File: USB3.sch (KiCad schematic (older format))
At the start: 45 parts

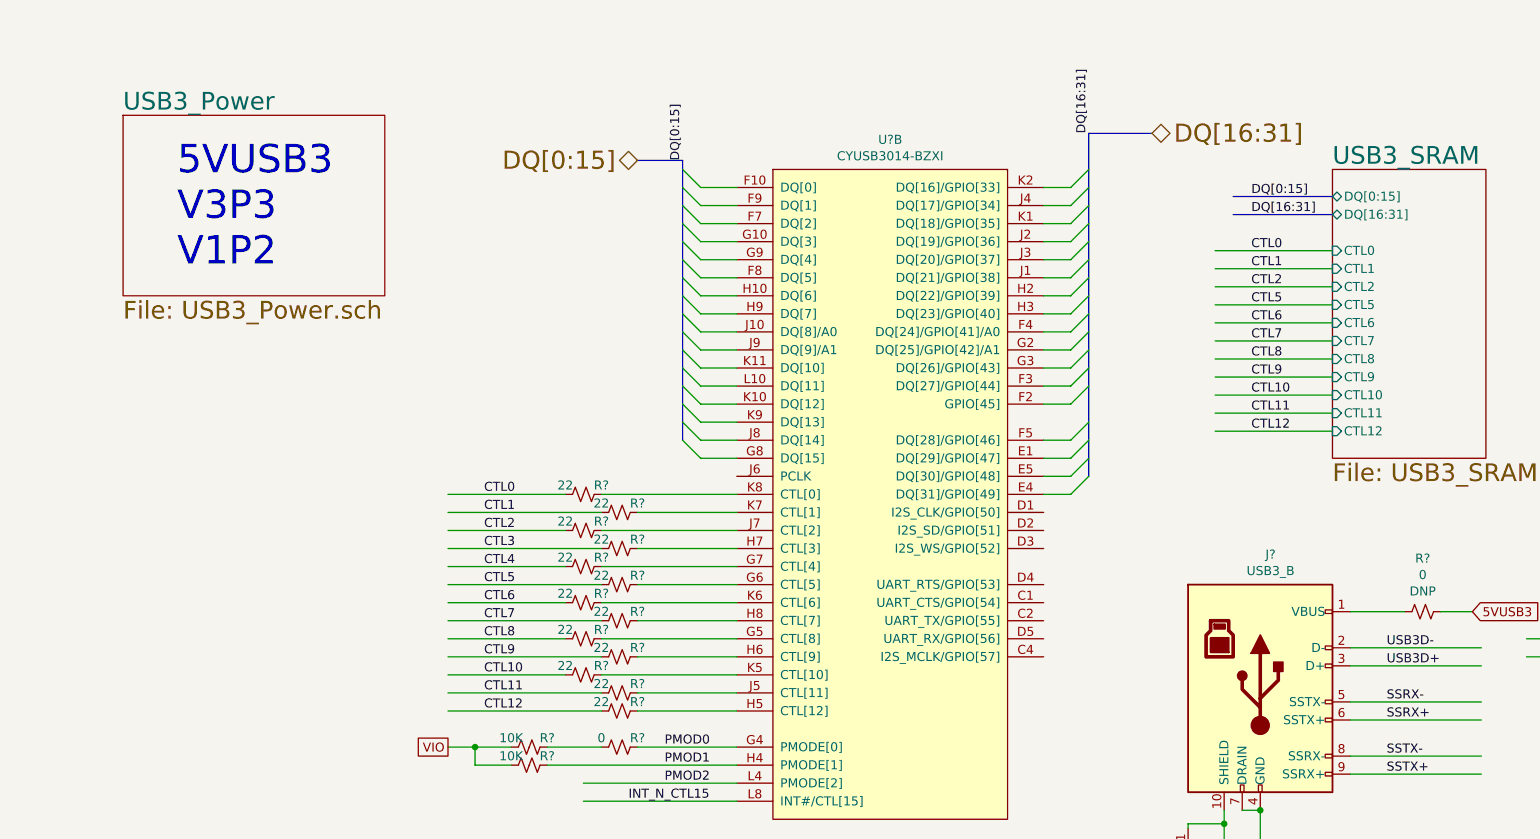
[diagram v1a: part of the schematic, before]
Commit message: Rearranged the top sheet blocks modified hir. pins in few blocks
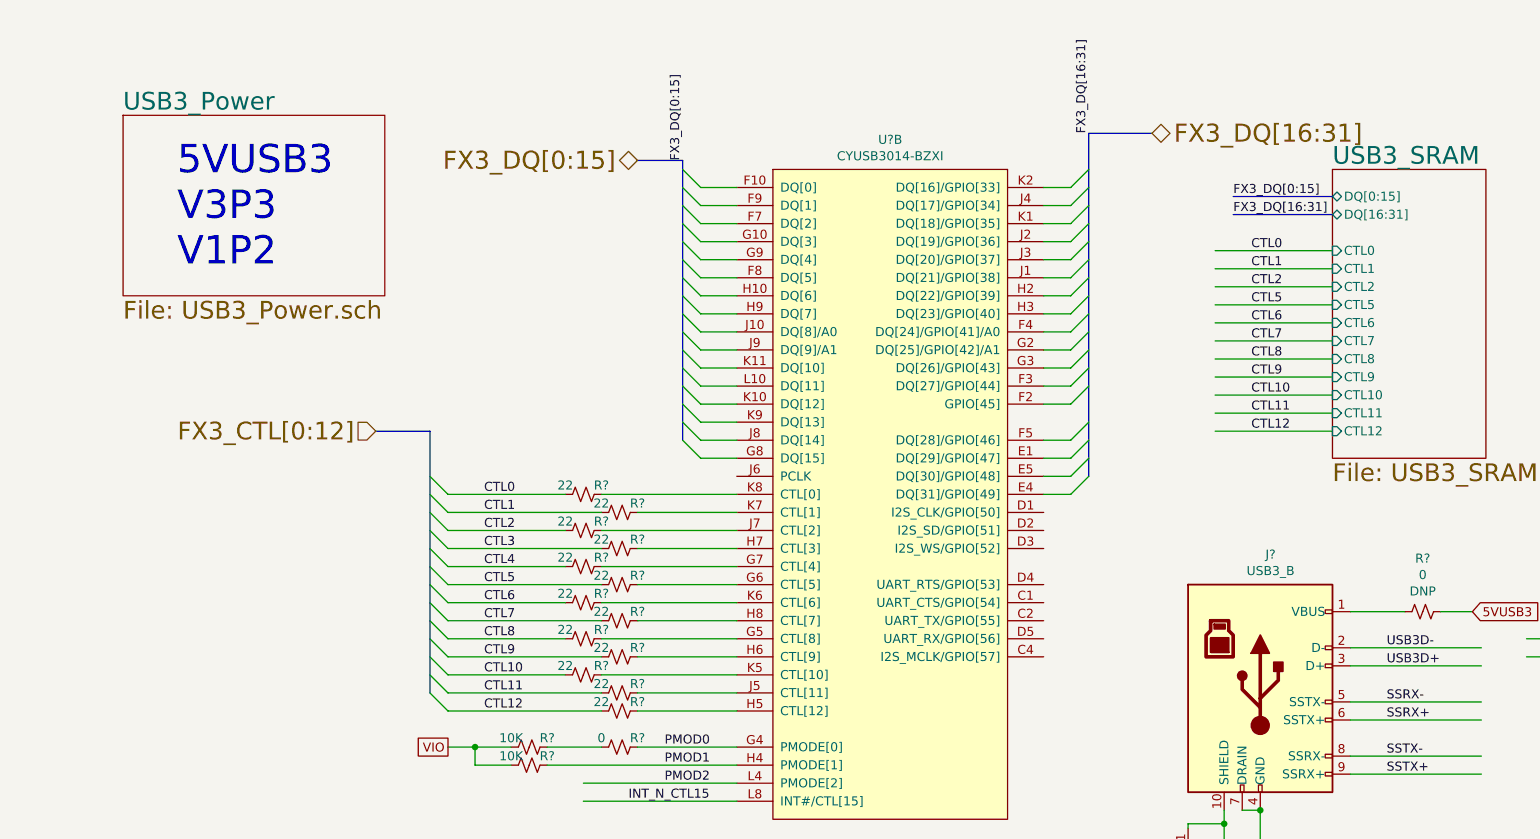
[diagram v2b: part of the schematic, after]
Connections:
- net labels added: FX3_CTL[0:12], FX3_DQ[0:15], FX3_DQ[16:31]
- net labels removed: DQ[0:15], DQ[16:31]
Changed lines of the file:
@@
 $Descr A4 11693 8268
 encoding utf-8
-Sheet 15 22
+Sheet 13 22
 Title "CGMPCX1006"
 Date "2021-02-03"
@@
 	6100 1050 6450 1050
 Text HLabel 6450 1050 2    100  BiDi ~ 0
-DQ[16:31]
+FX3_DQ[16:31]
 $Comp
 L GM_Memory_EEPROM:M24M02-DRMN6TP IC?
@@
 Text Notes 1050 1800 0    157  ~ 0
 5VUSB3\nV3P3\nV1P2
-Text Label 6100 1050 1    50   ~ 0
-DQ[16:31]
-Text Label 3850 1200 1    50   ~ 0
-DQ[0:15]
 Wire Bus Line
 	3850 1200 3600 1200
 Text HLabel 3600 1200 0    100  BiDi ~ 0
-DQ[0:15]
-Text Label 7000 1500 0    50   ~ 0
-DQ[16:31]
+FX3_DQ[0:15]
+Text Label 6900 1500 0    50   ~ 0
+FX3_DQ[16:31]
 Wire Bus Line
 	7450 1400 6900 1400
 Wire Bus Line
 	7450 1500 6900 1500
-Text Label 7000 1400 0    50   ~ 0
-DQ[0:15]
+Text Label 6900 1400 0    50   ~ 0
+FX3_DQ[0:15]
 $Comp
 L Device:R_Small_US R?
@@
 Wire Wire Line
 	5600 7300 5700 7300
+Text Label 6100 1050 1    50   ~ 0
+FX3_DQ[16:31]
+Text Label 3850 1200 1    50   ~ 0
+FX3_DQ[0:15]
+Entry Wire Line
+	2450 3950 2550 4050
+Entry Wire Line
+	2450 3850 2550 3950
+Entry Wire Line
+	2450 3750 2550 3850
+Entry Wire Line
+	2450 3650 2550 3750
+Entry Wire Line
+	2450 4050 2550 4150
+Entry Wire Line
+	2450 4150 2550 4250
+Entry Wire Line
+	2450 3350 2550 3450
+Entry Wire Line
+	2450 3250 2550 3350
+Entry Wire Line
+	2450 3150 2550 3250
+Entry Wire Line
+	2450 3050 2550 3150
+Entry Wire Line
+	2450 3450 2550 3550
+Entry Wire Line
+	2450 3550 2550 3650
+Entry Wire Line
+	2450 2950 2550 3050
+Wire Bus Line
+	2450 2700 2150 2700
+Wire Bus Line
+	2450 2700 2450 4150
 Wire Bus Line
 	3850 1200 3850 2750
 Wire Bus Line
 	6100 1050 6100 2950
+Text HLabel 2150 2700 0    98   Input ~ 0
+FX3_CTL[0:12]
 $EndSCHEMATC

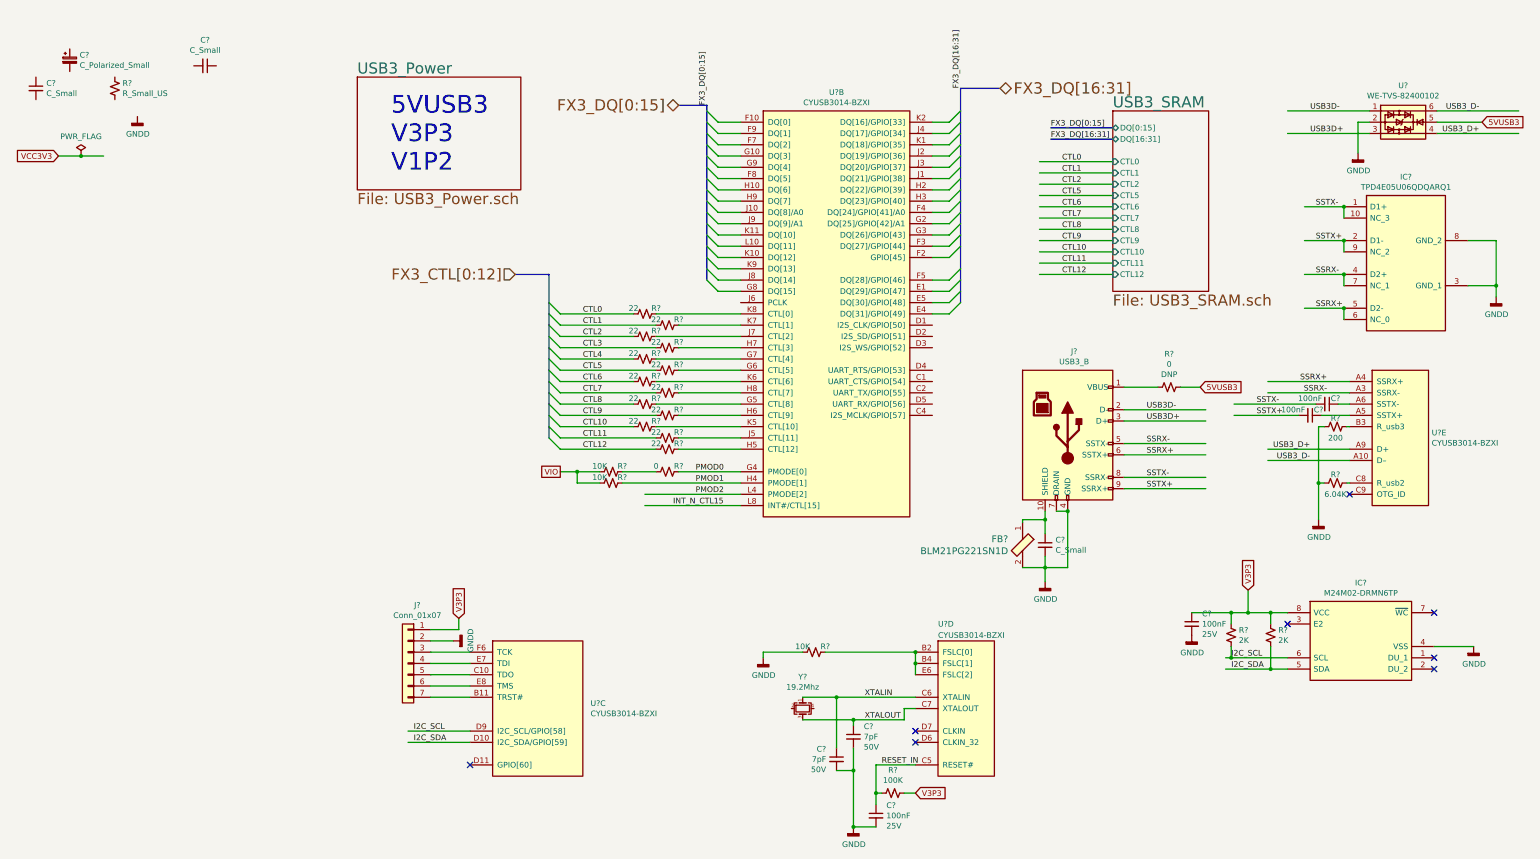
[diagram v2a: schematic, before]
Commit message: Added nets for fx3 usb3 cct from fpga
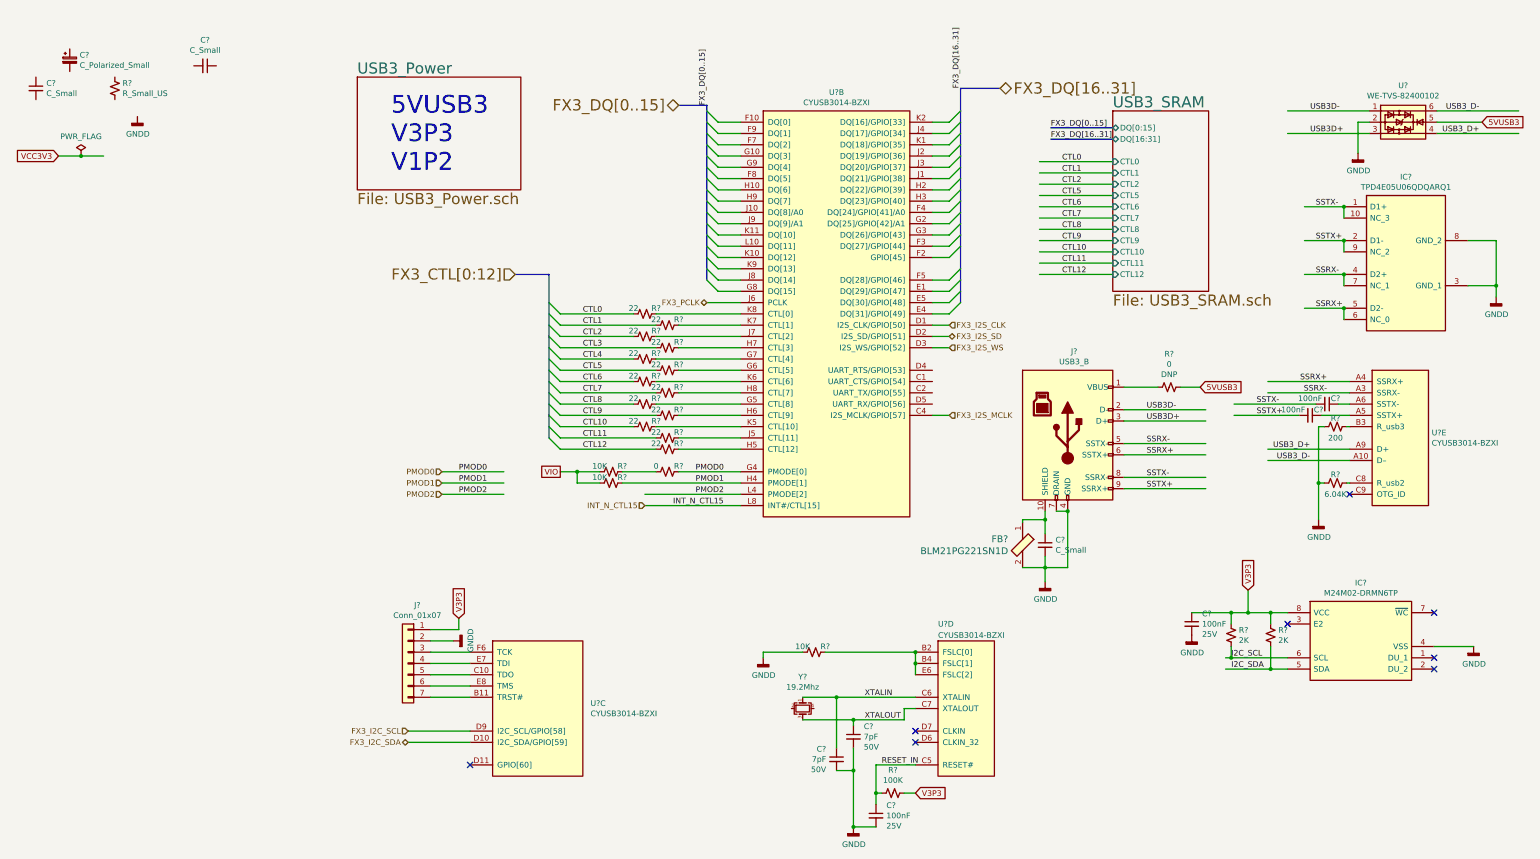
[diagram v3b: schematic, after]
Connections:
- net labels added: FX3_DQ[0..15], FX3_DQ[16..31], FX3_I2C_SCL, FX3_I2C_SDA, FX3_I2S_CLK, FX3_I2S_MCLK, FX3_I2S_SD, FX3_I2S_WS, FX3_PCLK
- net labels removed: FX3_DQ[0:15], FX3_DQ[16:31]
- wire segments 178 -> 186
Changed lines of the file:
@@
 Wire Bus Line
 	6100 1050 6450 1050
-Text HLabel 6450 1050 2    100  BiDi ~ 0
-FX3_DQ[16:31]
 $Comp
 L GM_Memory_EEPROM:M24M02-DRMN6TP IC?
@@
 Wire Wire Line
 	1750 6850 1200 6850
-Text Label 1250 6750 0    50   ~ 0
-I2C_SCL
-Text Label 1250 6850 0    50   ~ 0
-I2C_SDA
 Wire Wire Line
 	9000 6100 8500 6100
@@
 Wire Bus Line
 	3850 1200 3600 1200
-Text HLabel 3600 1200 0    100  BiDi ~ 0
-FX3_DQ[0:15]
-Text Label 6900 1500 0    50   ~ 0
-FX3_DQ[16:31]
 Wire Bus Line
 	7450 1400 6900 1400
 Wire Bus Line
 	7450 1500 6900 1500
-Text Label 6900 1400 0    50   ~ 0
-FX3_DQ[0:15]
 $Comp
 L Device:R_Small_US R?
@@
 Wire Wire Line
 	5600 7300 5700 7300
-Text Label 6100 1050 1    50   ~ 0
-FX3_DQ[16:31]
-Text Label 3850 1200 1    50   ~ 0
-FX3_DQ[0:15]
 Entry Wire Line
 	2450 3950 2550 4050
@@
 Wire Bus Line
 	2450 2700 2150 2700
+Text HLabel 2150 2700 0    98   Input ~ 0
+FX3_CTL[0:12]
+Text HLabel 1200 6750 0    50   Input ~ 0
+FX3_I2C_SCL
+Text HLabel 1200 6850 0    50   BiDi ~ 0
+FX3_I2C_SDA
+Wire Wire Line
+	4150 2950 3850 2950
+Text HLabel 3850 2950 0    50   BiDi ~ 0
+FX3_PCLK
+Text HLabel 6000 3150 2    50   Input ~ 0
+FX3_I2S_CLK
+Text HLabel 6000 3250 2    50   BiDi ~ 0
+FX3_I2S_SD
+Text HLabel 6000 3350 2    50   Input ~ 0
+FX3_I2S_WS
+Text HLabel 6000 3950 2    50   Input ~ 0
+FX3_I2S_MCLK
+Wire Wire Line
+	5850 3150 6000 3150
+Wire Wire Line
+	5850 3250 6000 3250
+Wire Wire Line
+	5850 3350 6000 3350
+Wire Wire Line
+	5850 3950 6000 3950
+Wire Wire Line
+	2050 4450 1500 4450
+Text Label 1650 4450 0    50   ~ 0
+PMOD0
+Text Label 1650 4550 0    50   ~ 0
+PMOD1
+Text Label 1650 4650 0    50   ~ 0
+PMOD2
+Wire Wire Line
+	2050 4550 1500 4550
+Wire Wire Line
+	2050 4650 1500 4650
 Wire Bus Line
 	2450 2700 2450 4150
@@
 Wire Bus Line
 	6100 1050 6100 2950
-Text HLabel 2150 2700 0    98   Input ~ 0
-FX3_CTL[0:12]
+Text HLabel 1500 4450 0    50   Input ~ 0
+PMOD0
+Text HLabel 1500 4550 0    50   Input ~ 0
+PMOD1
+Text HLabel 1500 4650 0    50   Input ~ 0
+PMOD2
+Text HLabel 3300 4750 0    50   Input ~ 0
+INT_N_CTL15
+Text Label 6900 1500 0    50   ~ 0
+FX3_DQ[16..31]
+Text Label 6900 1400 0    50   ~ 0
+FX3_DQ[0..15]
+Text Label 3850 1200 1    50   ~ 0
+FX3_DQ[0..15]
+Text Label 6100 1050 1    50   ~ 0
+FX3_DQ[16..31]
+Text HLabel 6450 1050 2    100  BiDi ~ 0
+FX3_DQ[16..31]
+Text HLabel 3600 1200 0    100  BiDi ~ 0
+FX3_DQ[0..15]
 $EndSCHEMATC

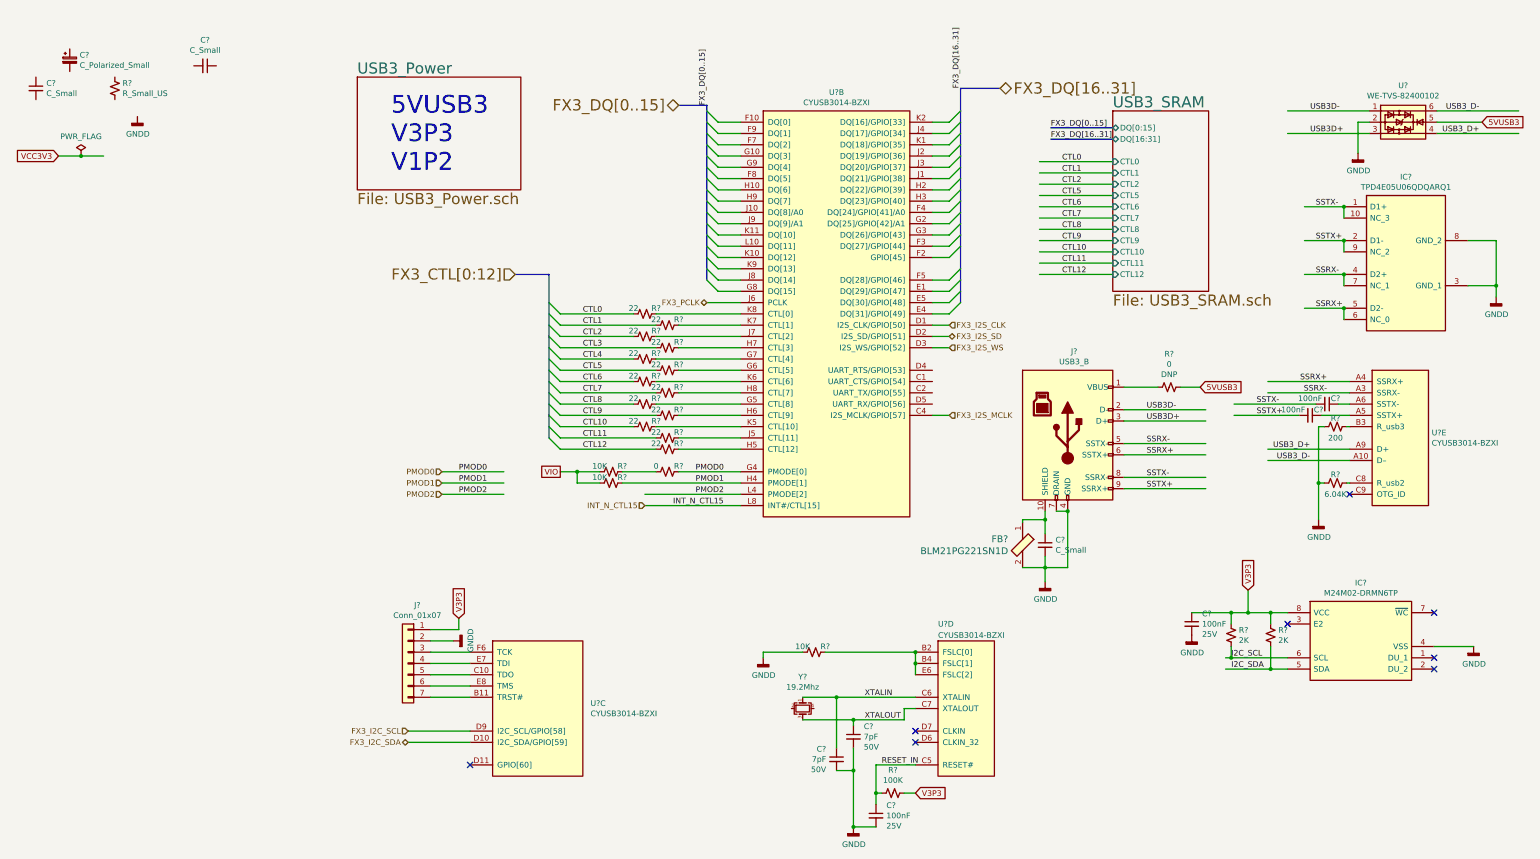
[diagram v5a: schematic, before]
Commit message: PCB created and schematics annotated High speed connections added to the BTB
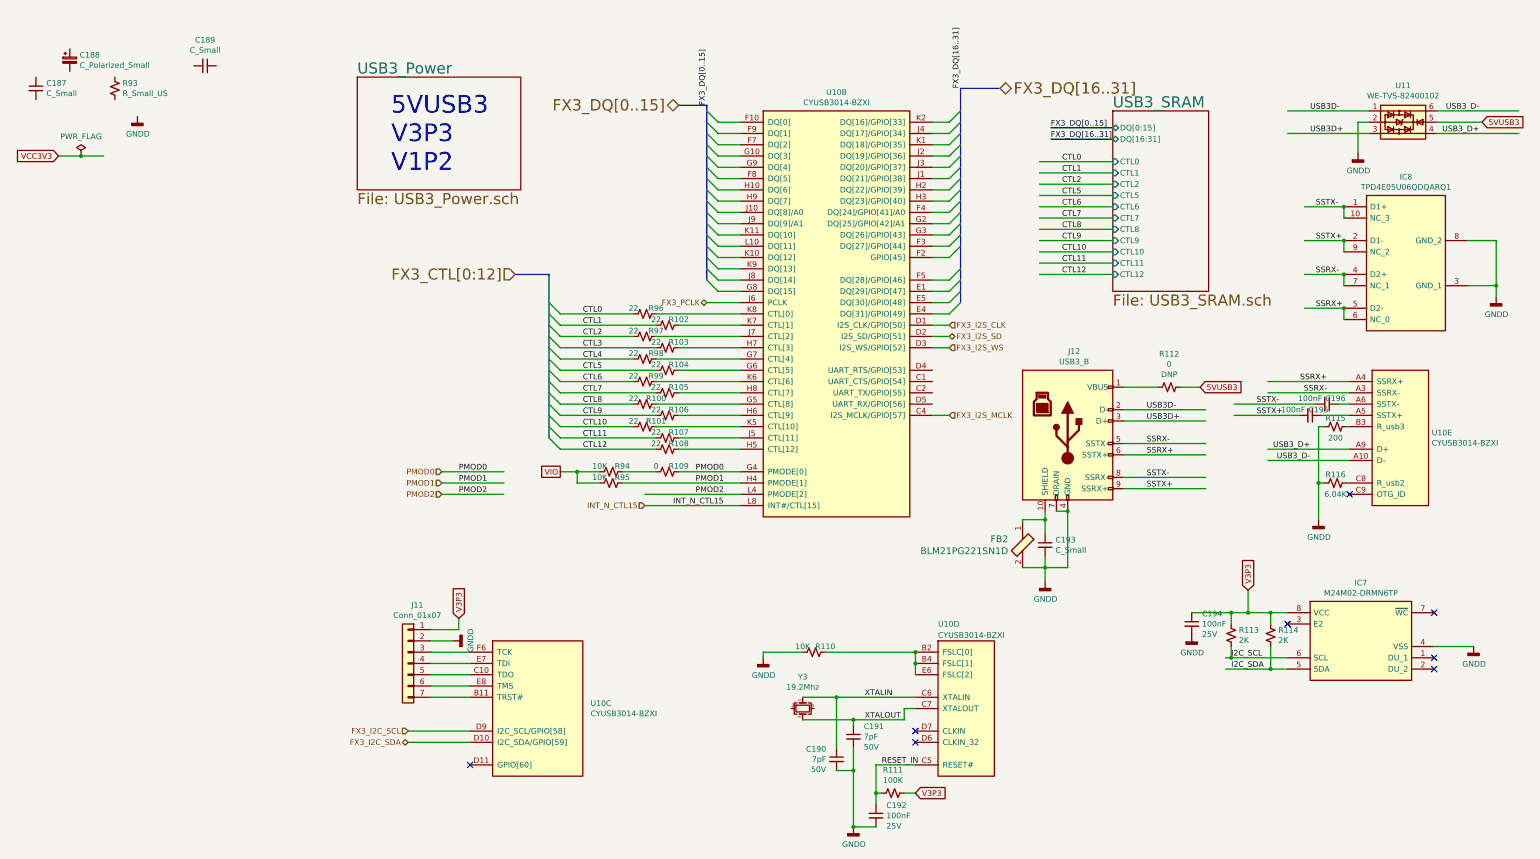
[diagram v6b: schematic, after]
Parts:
- gave numbers to parts that had none: 42
